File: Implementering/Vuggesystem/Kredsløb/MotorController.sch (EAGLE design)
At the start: 31 parts, among them IC1 74HC08N, IC2 74HC04N

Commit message: felix
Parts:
- C7, C8: value 22uF -> 1.2pF
- R10, R9: value 10 Ohm -> 3.3 kOhm
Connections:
- removed net N$11: IC1B.O, IC2C.I
- removed net N$14: IC1A.I1, IC2A.I, R9.1
- removed net N$17: IC2B.O
- removed net N$18: IC2C.O
- removed net N$19: IC1B.I0, IC2A.O, R10.1
- removed net VSS_A: C1.2, IO1.VSS, R5.2, U$1.S, U$4.D, X1-2.KL
- removed net VSS_B: C5.2, IO2.VSS, R8.1, U$2.D, U$3.S, X1-1.KL
- new net MOT_A: C1.2, IO1.VSS, R5.2, U$1.S, U$4.D, X1-1.KL
- new net MOT_B: C5.2, IO2.VSS, R8.1, U$2.D, U$3.S, X1-2.KL
- net +3V3: now also IC2C.I, IC2D.I, IC2E.I, IC2F.I
- net GND: now also IC1C.I0, IC1C.I1, IC1D.I0, IC1D.I1, SV1.1
- net M_A: now also IC1A.O, IO1.LIN; no longer IO2.HIN
- net M_AL: now also IO1.LO; no longer IO2.LO
- net M_B: now also IC1B.O, IO2.HIN; no longer IO1.LIN
- net M_BL: now also IO2.LO; no longer IO1.LO
- net N$10: now also IC1B.I0, IC2A.I, IC2B.O, R10.1; no longer IC1A.O, IC2B.I
- net PWM: now also IC1A.I1, IC2A.O, IC2B.I, R9.1
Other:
- note added: "Stik"
- note added: "Ubrugte elementer"
- moved on the sheet: C1, C2, C3, C4, C5, C6, C7, C8, D1, D2, IC1A, IC1B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

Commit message: har lavet print til motor kreds, og lavet lidt på motor kontrol -Felix
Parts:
- removed C7, C8: 1.2pF, SparkFun-Passives:CAPPTH1
- removed IC1: 74HC08N, 74xx-eu:74HC08N
- removed IC2: 74HC04N, 74xx-eu:74HC04N
- removed R10: 3.3 kOhm, rcl:R-EU_0207/10
- removed U$1, U$2, U$3, U$4: IRFZ24N, transistor-power:IRFZ24N
- added Q1, Q2, Q3, Q4: IRF512, transistor-power:IRF512
- added SV2: (no value), con-lstb:MA04-1
- R9: value 3.3 kOhm -> 10 Ohm
- SV1: device con-lstb:MA03-1 -> con-lstb:MA05-1
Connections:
- removed net N$10: IC1B.I0, IC2A.I, IC2B.O, R10.1
- removed net N$15: C7.1, IC1A.I0, R9.2
- removed net N$16: C8.1, IC1B.I1, R10.2
- removed net PWM: IC1A.I1, IC2A.O, IC2B.I, R9.1, SV1.2
- new net ES_SIG: R9.1, SV1.4, SV2.1, SV2.3
- net +3V3: now also R9.2, SV1.5; no longer IC2C.I, IC2D.I, IC2E.I, IC2F.I, SV1.3
- net GND: now also Q2.S, Q3.S, SV2.2, SV2.4; no longer C7.2, C8.2, IC1C.I0, IC1C.I1, IC1D.I0, IC1D.I1, U$2.S, U$4.S
- net MOT_A: now also Q1.S, Q2.D; no longer U$1.S, U$4.D
- net MOT_B: now also Q3.D, Q4.S; no longer U$2.D, U$3.S
- net M_A: now also SV1.2; no longer IC1A.O
- net M_B: now also SV1.3; no longer IC1B.O
- net N$3: now also Q1.G; no longer U$1.G
- net N$4: now also Q2.G; no longer U$4.G
- net N$5: now also Q4.G; no longer U$3.G
- net N$6: now also Q3.G; no longer U$2.G
- net VCC: now also Q1.D, Q4.D; no longer U$1.D, U$3.D
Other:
- note added: "EndStop"
- note removed: "Dead-time kreds"
- note removed: "Ubrugte elementer"
- moved on the sheet: C3, C4, R1, R2, R3, R4, R5, R6, R7, R8, R9, X1-1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

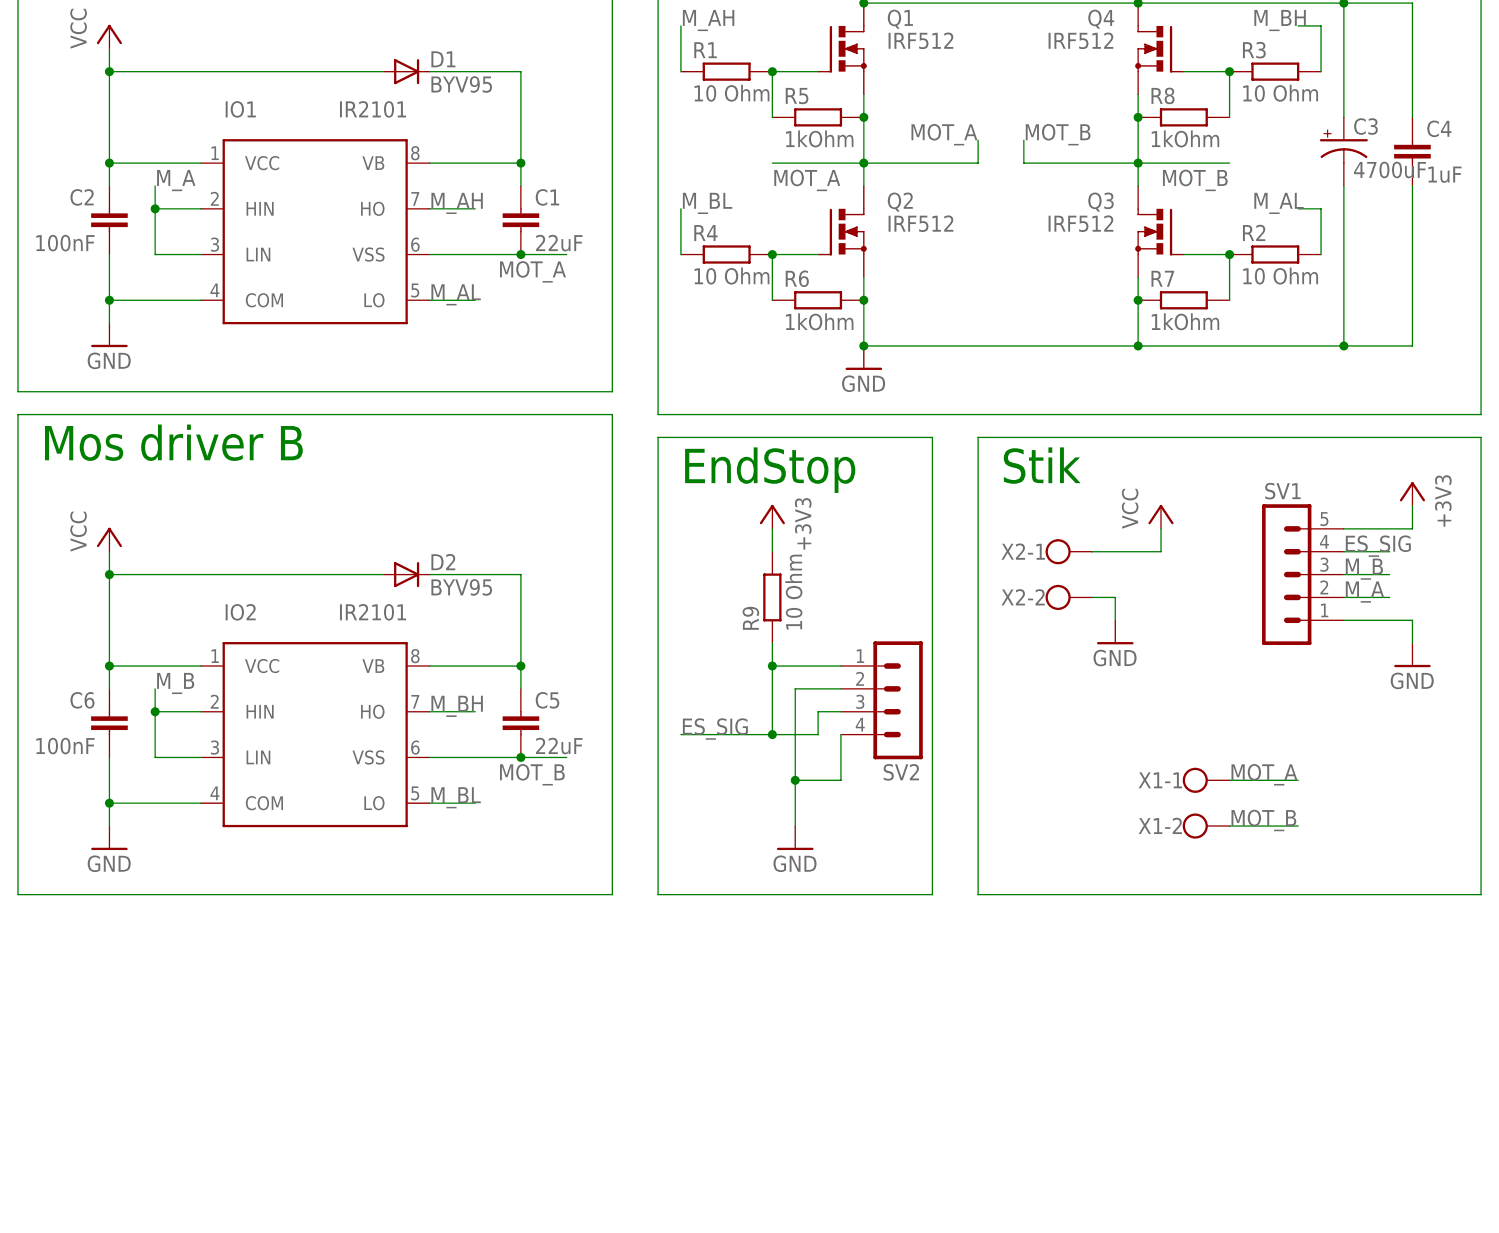
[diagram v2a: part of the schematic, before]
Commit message: VS: tilføjet optokobler afsnit -Felix
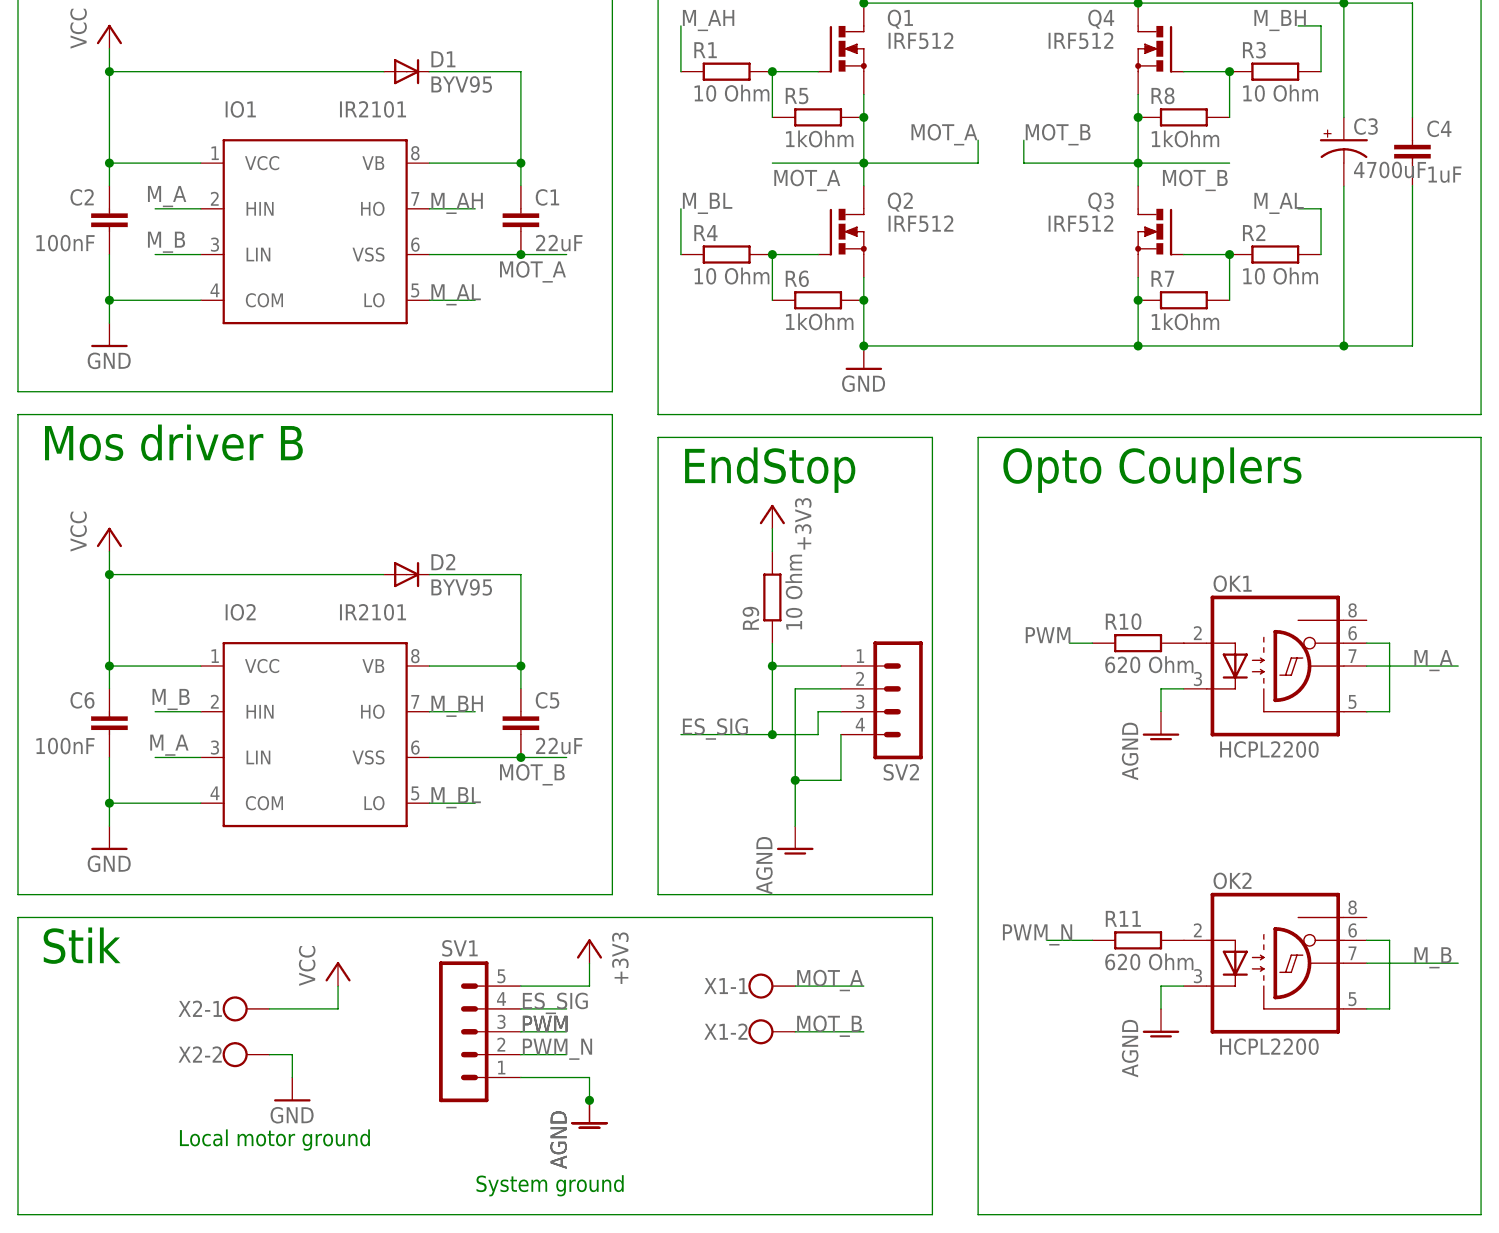
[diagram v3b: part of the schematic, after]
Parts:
- added OK1, OK2: HCPL2200, optocoupler:HCPL2200
- added R10, R11: 620 Ohm, rcl:R-EU_0207/10
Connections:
- new net AGND: OK1.C, OK2.C, SV1.1, SV2.2, SV2.4
- new net N$10: OK1.A, R10.2
- new net N$11: OK2.A, R11.2
- new net N$14: OK2.GND, OK2.VE
- new net N$16: OK1.GND, OK1.VE
- new net PWM: R10.1, SV1.3
- new net PWM_N: R11.1, SV1.2
- net GND: no longer SV1.1, SV2.2, SV2.4
- net M_A: now also IO2.LIN, OK1.VO; no longer IO1.LIN, SV1.2
- net M_B: now also IO1.LIN, OK2.VO; no longer IO2.LIN, SV1.3
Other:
- note added: "Local motor ground"
- note added: "Opto Couplers"
- note added: "System ground"
- moved on the sheet: SV1, X1-1, X1-2, X2-1, X2-2
